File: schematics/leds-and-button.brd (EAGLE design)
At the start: 40.3 x 17.8 mm, 10 parts

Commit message: Reworked the boards
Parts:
- removed JP4: (no value), SparkFun:1X02
- removed LED_12V, LED_3.3V, LED_5V, LED_9V, LED_ADJV: (no value), SparkFun:LED3MM-NS
- added 12V, 3.3V, 5V, 9V, ADJV: (no value), SparkFun:LED3MM-NS
- added BTN: (no value), SparkFun:1X02
- moved JP1 10.2 mm to (26.7, 3.81)
- moved JP3 7.62 mm to (20.3, 2.54), flipped to the bottom
- moved RN1 5.08 mm to (15.2, 12.7), flipped to the bottom
- moved JP2 1.80 mm to (3.81, 12.7)
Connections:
- net N$10: now also ADJV.K; no longer LED_ADJV.K
- net N$11: now also BTN.2; no longer JP4.2
- net N$12: now also BTN.1; no longer JP4.1
- net N$13: now also ADJV.A; no longer LED_ADJV.A
- net N$2: now also 3.3V.K; no longer LED_3.3V.K
- net N$3: now also 5V.K; no longer LED_5V.K
- net N$4: now also 3.3V.A; no longer LED_3.3V.A
- net N$5: now also 5V.A; no longer LED_5V.A
- net N$6: now also 9V.A; no longer LED_9V.A
- net N$7: now also 12V.A; no longer LED_12V.A
- net N$8: now also 9V.K; no longer LED_9V.K
- net N$9: now also 12V.K; no longer LED_12V.K
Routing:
- net N$2: track 4.86 -> 22.7 mm
- net N$13: track 5.39 -> 22.8 mm
- net N$11: track 0.00 -> 13.6 mm
- net N$12: track 0.00 -> 13.6 mm
- net N$3: track 3.81 -> 14.0 mm
- net N$7: track 4.34 -> 12.9 mm
- net N$4: track 7.93 -> 15.3 mm
- net N$10: track 9.20 -> 14.1 mm
- net N$1: track 17.2 -> 12.8 mm
- net N$5: track 5.39 -> 6.69 mm
- net N$9: track 6.66 -> 5.47 mm
- net N$8: track 4.86 -> 5.41 mm
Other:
- board size 40.3 x 17.8 mm -> 30.1 x 16.5 mm

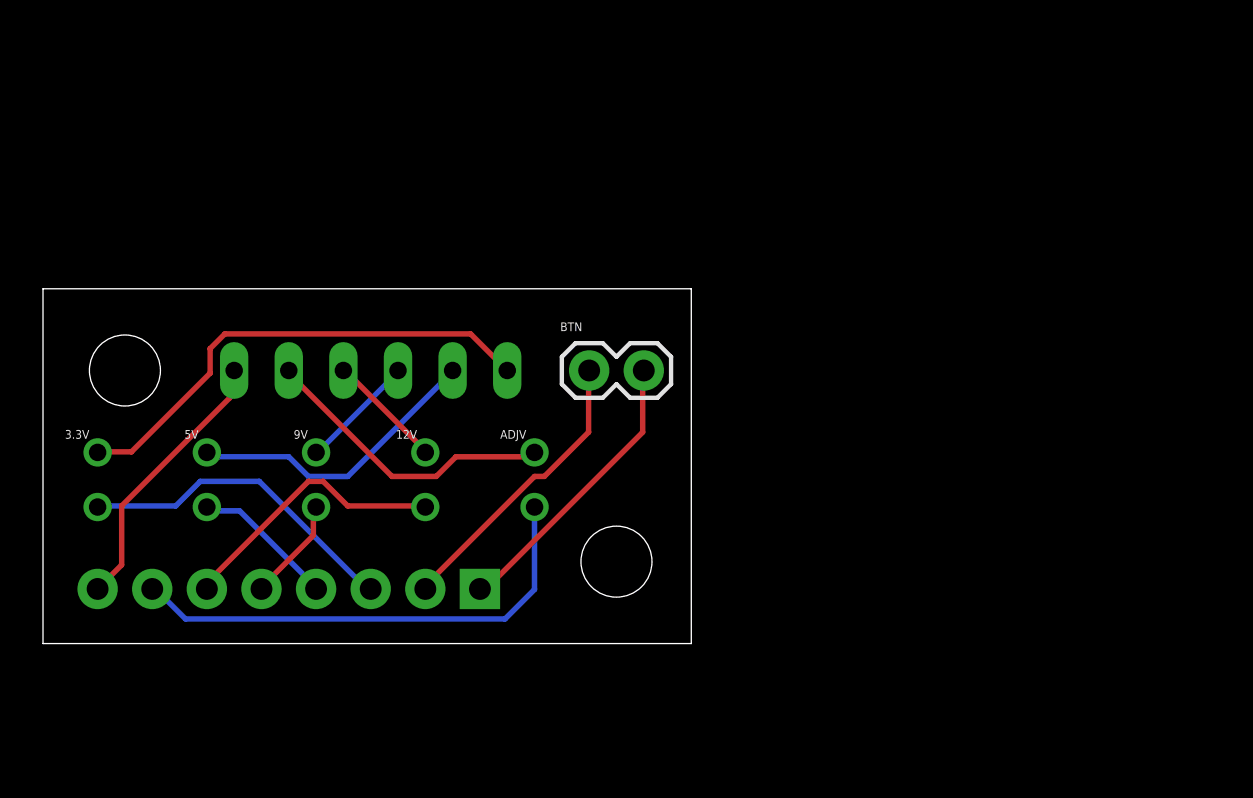
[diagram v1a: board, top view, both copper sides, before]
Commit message: Moved the shift register to the top board since I have more room there and on the bottom board and I get to free up some pins on the jumper
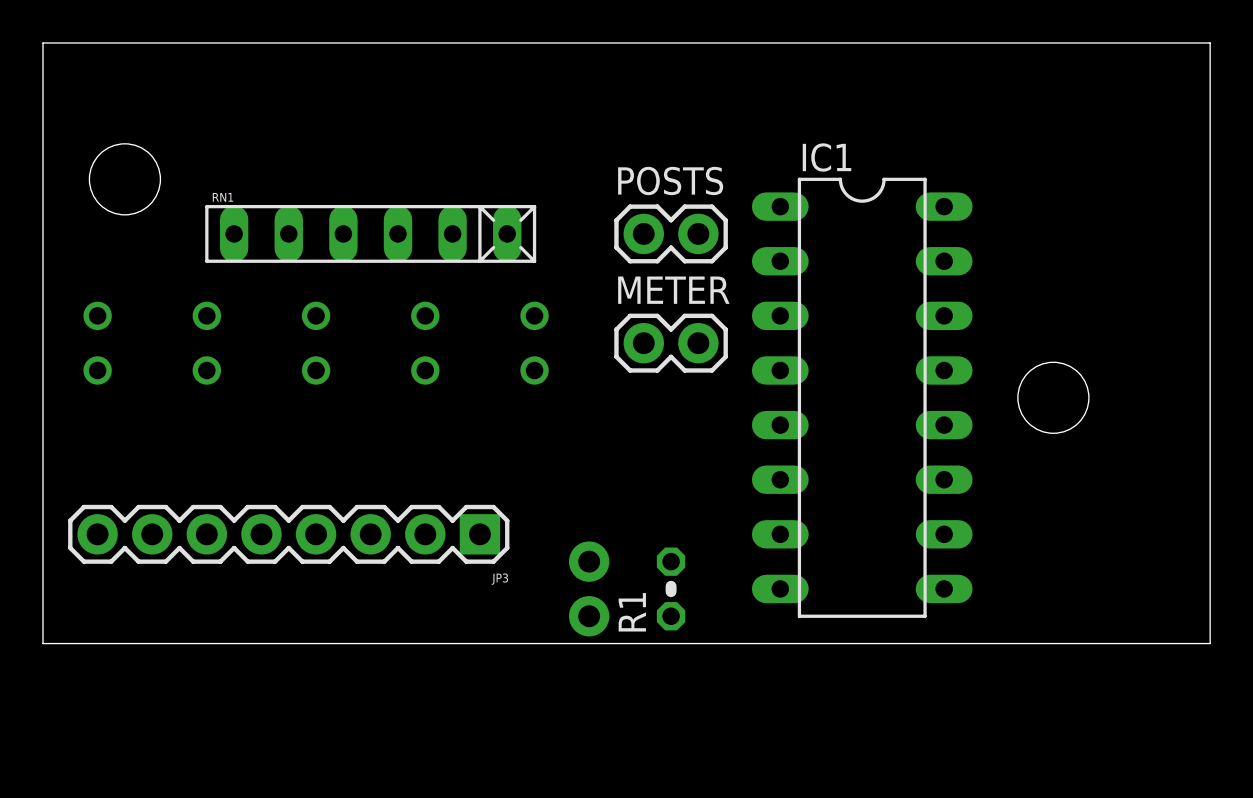
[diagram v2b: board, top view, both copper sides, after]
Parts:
- added IC1: 74LS595N, 74xx-us:DIL16
- added METER, POSTS: (no value), SparkFun:1X02
- added R1: 10k, resistor:0204V
- moved JP1 21.7 mm to (47.0, 11.4)
- moved 3.3V 21.3 mm to (22.9, 14.0), flipped to the bottom
- moved ADJV 21.3 mm to (2.54, 14.0), flipped to the bottom
- moved 12V 12.0 mm to (7.62, 14.0), flipped to the bottom
- moved 5V 12.0 mm to (17.8, 14.0), flipped to the bottom
- moved JP2 8.89 mm to (3.81, 21.6)
- moved BTN 8.89 mm to (25.4, 3.81), flipped to the bottom, turned to 270 degrees
- moved RN1 6.35 mm to (15.2, 19.1), flipped to the top
- moved 9V 6.35 mm to (12.7, 14.0), flipped to the bottom
- moved JP3 2.54 mm to (20.3, 5.08), flipped to the top, turned to 180 degrees
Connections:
- net N$11 renamed IC_VCC
- removed net N$1: JP3.8, RN1.1
- removed net N$12: BTN.1, JP3.2
- new net GND: IC1.8, JP3.8, METER.2, POSTS.2, R1.2, RN1.1
- new net N$11: IC1.13, IC1.9, R1.1
- new net PB0: BTN.1, JP3.3
- new net PB1: IC1.14, JP3.4
- new net PB2: IC1.12, JP3.5
- new net PB3: IC1.11, JP3.6
- new net PB4: IC1.10, JP3.7
- new net VCC: IC1.16, JP3.2, METER.1, POSTS.1
- net N$10: now also 3.3V.K; no longer ADJV.K
- net N$13: now also 3.3V.A, IC1.1; no longer ADJV.A, JP3.7
- net N$2: now also ADJV.K; no longer 3.3V.K
- net N$3: now also 12V.K; no longer 5V.K
- net N$4: now also ADJV.A, IC1.5; no longer 3.3V.A, JP3.3
- net N$5: now also 12V.A, IC1.4; no longer 5V.A, JP3.4
- net N$6: now also IC1.3; no longer JP3.5
- net N$7: now also 5V.A, IC1.2; no longer 12V.A, JP3.6
- net N$9: now also 5V.K; no longer 12V.K
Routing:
- net N$13: track 22.8 -> 0.00 mm
- net N$2: track 22.7 -> 0.00 mm
- net N$4: track 15.3 -> 0.00 mm
- net N$10: track 14.1 -> 0.00 mm
- net N$3: track 14.0 -> 0.00 mm
- net IC_VCC: track 13.6 -> 0.00 mm
- net N$12: track 13.6 -> 0.00 mm
- net N$7: track 12.9 -> 0.00 mm
- net N$1: track 12.8 -> 0.00 mm
- net N$5: track 6.69 -> 0.00 mm
- net N$9: track 5.47 -> 0.00 mm
- net N$8: track 5.41 -> 0.00 mm
- net N$6: track 4.83 -> 0.00 mm
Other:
- board size 30.1 x 16.5 mm -> 54.3 x 27.9 mm

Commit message: Updated the schematics
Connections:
- net IC_VCC: now also IC1.10
- net PB2: now also IC1.11; no longer IC1.12
- net PB3: now also IC1.12; no longer IC1.11
- net PB4: no longer IC1.10
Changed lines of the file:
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@@
 <contactref element="JP3" pad="1"/>
 <contactref element="BTN" pad="2"/>
-<wire x1="25.4" y1="1.27" x2="20.32" y2="5.08" width="0" layer="19" extent="1-1"/>
+<contactref element="IC1" pad="10"/>
+<wire x1="25.4" y1="1.27" x2="41.91" y2="5.08" width="0" layer="19" extent="1-1"/>
+<wire x1="20.32" y1="5.08" x2="25.4" y2="1.27" width="0" layer="19" extent="1-1"/>
 </signal>
 <signal name="GND">
@@
 </signal>
 <signal name="PB3">
-<contactref element="IC1" pad="11"/>
 <contactref element="JP3" pad="6"/>
-<wire x1="7.62" y1="5.08" x2="41.91" y2="7.62" width="0" layer="19" extent="1-1"/>
+<contactref element="IC1" pad="12"/>
+<wire x1="7.62" y1="5.08" x2="41.91" y2="10.16" width="0" layer="19" extent="1-1"/>
 </signal>
 <signal name="PB4">
-<contactref element="IC1" pad="10"/>
 <contactref element="JP3" pad="7"/>
-<wire x1="5.08" y1="5.08" x2="41.91" y2="5.08" width="0" layer="19" extent="1-1"/>
 </signal>
 <signal name="PB2">
-<contactref element="IC1" pad="12"/>
 <contactref element="JP3" pad="5"/>
-<wire x1="10.16" y1="5.08" x2="41.91" y2="10.16" width="0" layer="19" extent="1-1"/>
+<contactref element="IC1" pad="11"/>
+<wire x1="10.16" y1="5.08" x2="41.91" y2="7.62" width="0" layer="19" extent="1-1"/>
 </signal>
 </signals>

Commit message: Played around with the board for the leds
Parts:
- removed JP1: STAND-OFF, SparkFun:STAND-OFF
- 12V, 3.3V, 5V, 9V, ADJV: device SparkFun:LED3MM-NS -> SparkFun-LED:LED3MM
- moved METER 25.7 mm to (2.54, 17.8)
- moved JP2 20.5 mm to (22.9, 14.0)
- moved POSTS 19.1 mm to (8.89, 17.8)
- moved BTN 17.3 mm to (15.2, 17.8), flipped to the top, turned to 0 degrees
- moved RN1 8.98 mm to (8.89, 12.7)
- moved IC1 6.35 mm to (31.8, 11.4)
- moved 12V 6.35 mm to (7.62, 7.62)
- moved 3.3V 6.35 mm to (22.9, 7.62)
- moved 5V 6.35 mm to (17.8, 7.62)
- moved 9V 6.35 mm to (12.7, 7.62)
- moved ADJV 6.35 mm to (2.54, 7.62)
- moved R1 5.08 mm to (24.1, 2.54), turned to 270 degrees
- moved JP3 2.54 mm to (20.3, 2.54)
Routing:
- net PB2: track 0.00 -> 61.1 mm, vias 0 -> 4
- net VCC: track 0.00 -> 57.2 mm, vias 0 -> 1
- net GND: track 0.00 -> 56.9 mm
- net IC_VCC: track 0.00 -> 44.7 mm
- net N$5: track 0.00 -> 37.5 mm, vias 0 -> 2
- net N$6: track 0.00 -> 36.8 mm, vias 0 -> 1
- net N$4: track 0.00 -> 33.6 mm
- net PB3: track 0.00 -> 31.1 mm
- net N$11: track 0.00 -> 26.6 mm, vias 0 -> 1
- net N$13: track 0.00 -> 17.0 mm
- net N$7: track 0.00 -> 16.6 mm
- net PB0: track 0.00 -> 16.1 mm
- net N$9: track 0.00 -> 11.8 mm
- net N$8: track 0.00 -> 9.19 mm
- net N$3: track 0.00 -> 6.64 mm
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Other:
- board size 54.3 x 27.9 mm -> 37.8 x 22.9 mm
- board text added: "20151022"
- board text added: "Indicators and Selector"

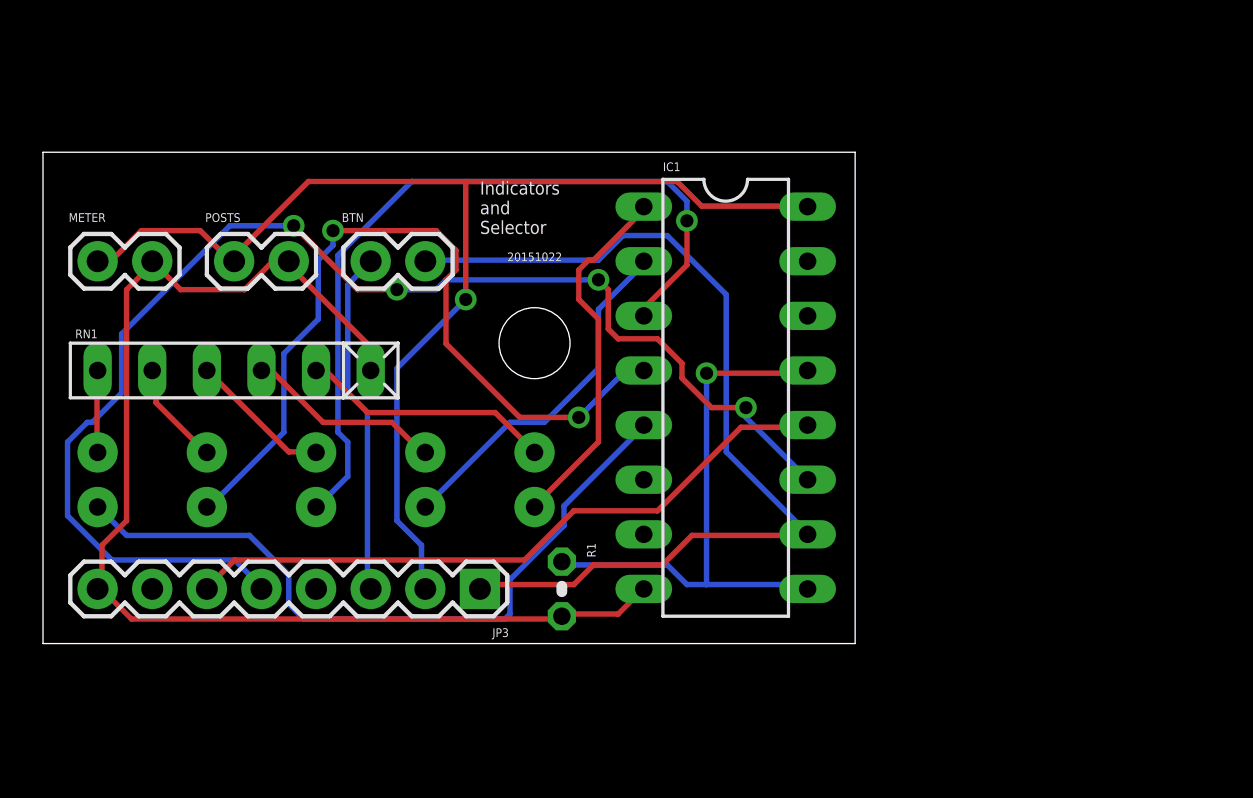
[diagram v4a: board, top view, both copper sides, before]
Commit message: Decided to remove the "adjustable" option because it was kinda useless
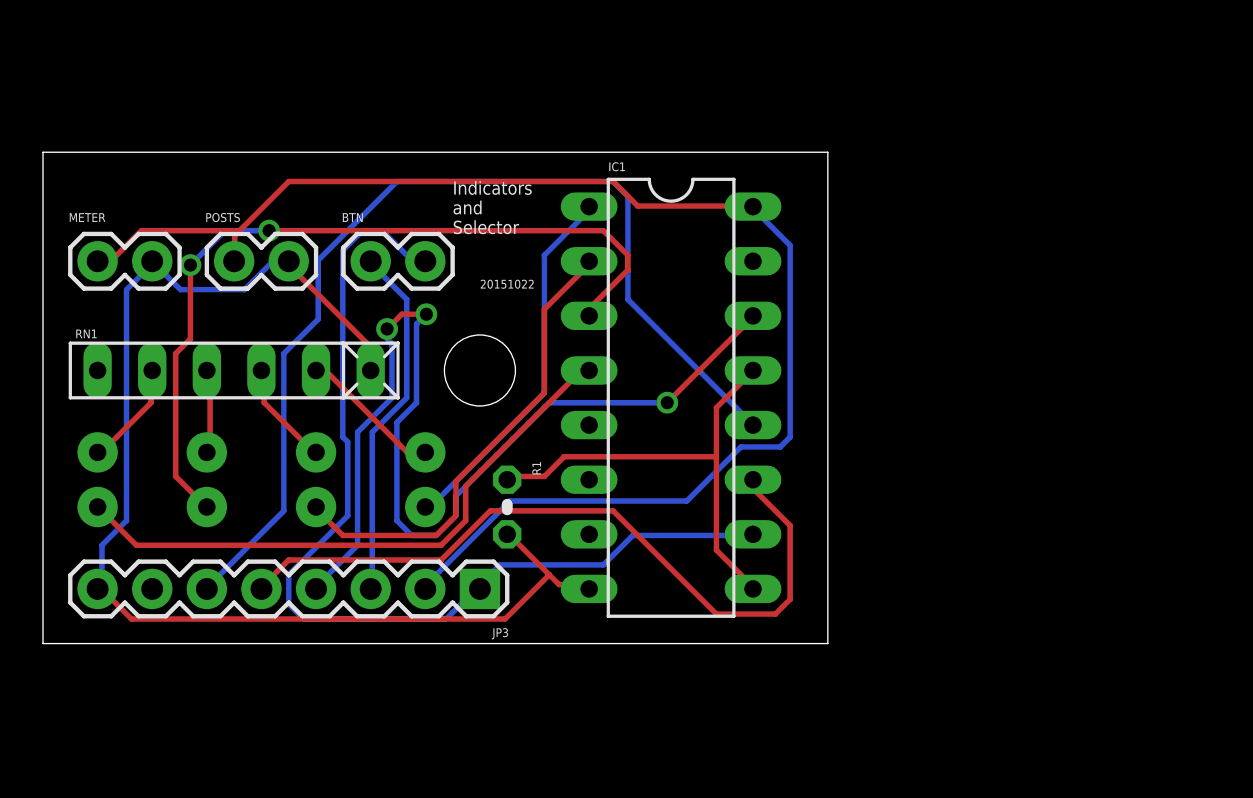
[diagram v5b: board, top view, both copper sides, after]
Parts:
- removed ADJV: (no value), SparkFun-LED:LED3MM
- moved 5V 5.08 mm to (12.7, 7.62)
- moved 12V 5.08 mm to (2.54, 7.62)
- moved 9V 5.08 mm to (7.62, 7.62)
- moved 3.3V 5.08 mm to (17.8, 7.62)
- moved R1 4.58 mm to (21.6, 6.35)
- moved JP2 2.84 mm to (20.3, 12.7)
- moved IC1 2.54 mm to (29.2, 11.4)
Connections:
- removed net N$1: ADJV.K, RN1.6
- removed net N$4: ADJV.A, IC1.5
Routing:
- net PB1: track 0.00 -> 47.5 mm, vias 0 -> 3
- net N$4: track 33.6 -> 0.00 mm
- net PB2: track 61.1 -> 34.7 mm, vias 4 -> 0
- net PB3: track 31.1 -> 46.7 mm
- net N$5: track 37.5 -> 27.9 mm, vias 2 -> 0
- net VCC: track 57.2 -> 65.4 mm, vias 1 -> 0
- net N$7: track 16.6 -> 21.9 mm
- net N$9: track 11.8 -> 6.66 mm
- net N$11: track 26.6 -> 21.7 mm, vias 1 -> 0
- net N$8: track 9.19 -> 4.91 mm
- net N$1: track 3.82 -> 0.00 mm
- net N$3: track 6.64 -> 4.01 mm
- net IC_VCC: track 44.7 -> 46.1 mm
- net GND: track 56.9 -> 57.9 mm
- net N$13: track 17.0 -> 17.5 mm
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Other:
- board size 37.8 x 22.9 mm -> 36.5 x 22.9 mm

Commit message: Tweak tweak
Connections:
- net IC_VCC renamed VIC
- net VCC renamed VADJ
- removed net PB4: JP3.7
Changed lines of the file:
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@@
 <wire x1="17.8308" y1="6.1722" x2="17.78" y2="6.35" width="0.254" layer="16"/>
 </signal>
-<signal name="IC_VCC">
+<signal name="VIC">
 <contactref element="JP3" pad="1"/>
 <contactref element="BTN" pad="2"/>
@@
 <wire x1="11.43" y1="17.6022" x2="11.43" y2="17.78" width="0.254" layer="16"/>
 </signal>
-<signal name="VCC">
+<signal name="VADJ">
 <contactref element="IC1" pad="16"/>
 <contactref element="JP3" pad="2"/>
@@
 <wire x1="7.7724" y1="2.7432" x2="7.62" y2="2.54" width="0.254" layer="16"/>
 </signal>
-<signal name="PB4">
-<contactref element="JP3" pad="7"/>
-</signal>
 <signal name="PB2">
